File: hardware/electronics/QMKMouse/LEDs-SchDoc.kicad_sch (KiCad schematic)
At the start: 20 parts

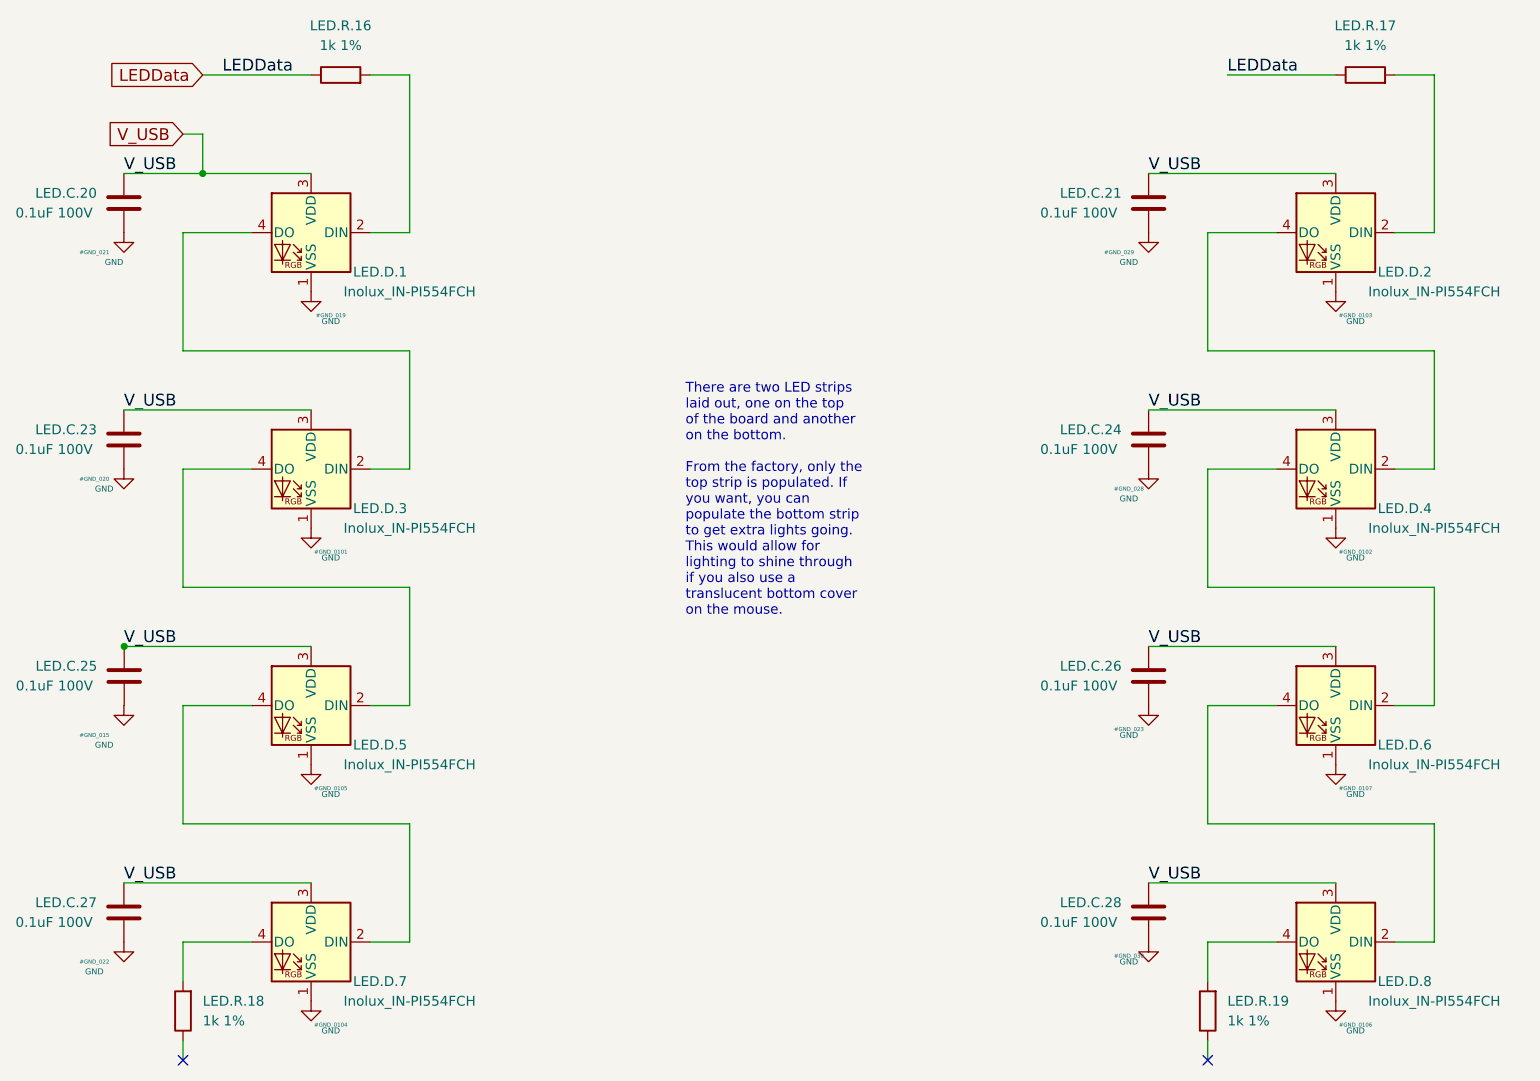
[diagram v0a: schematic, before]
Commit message: update schematic components
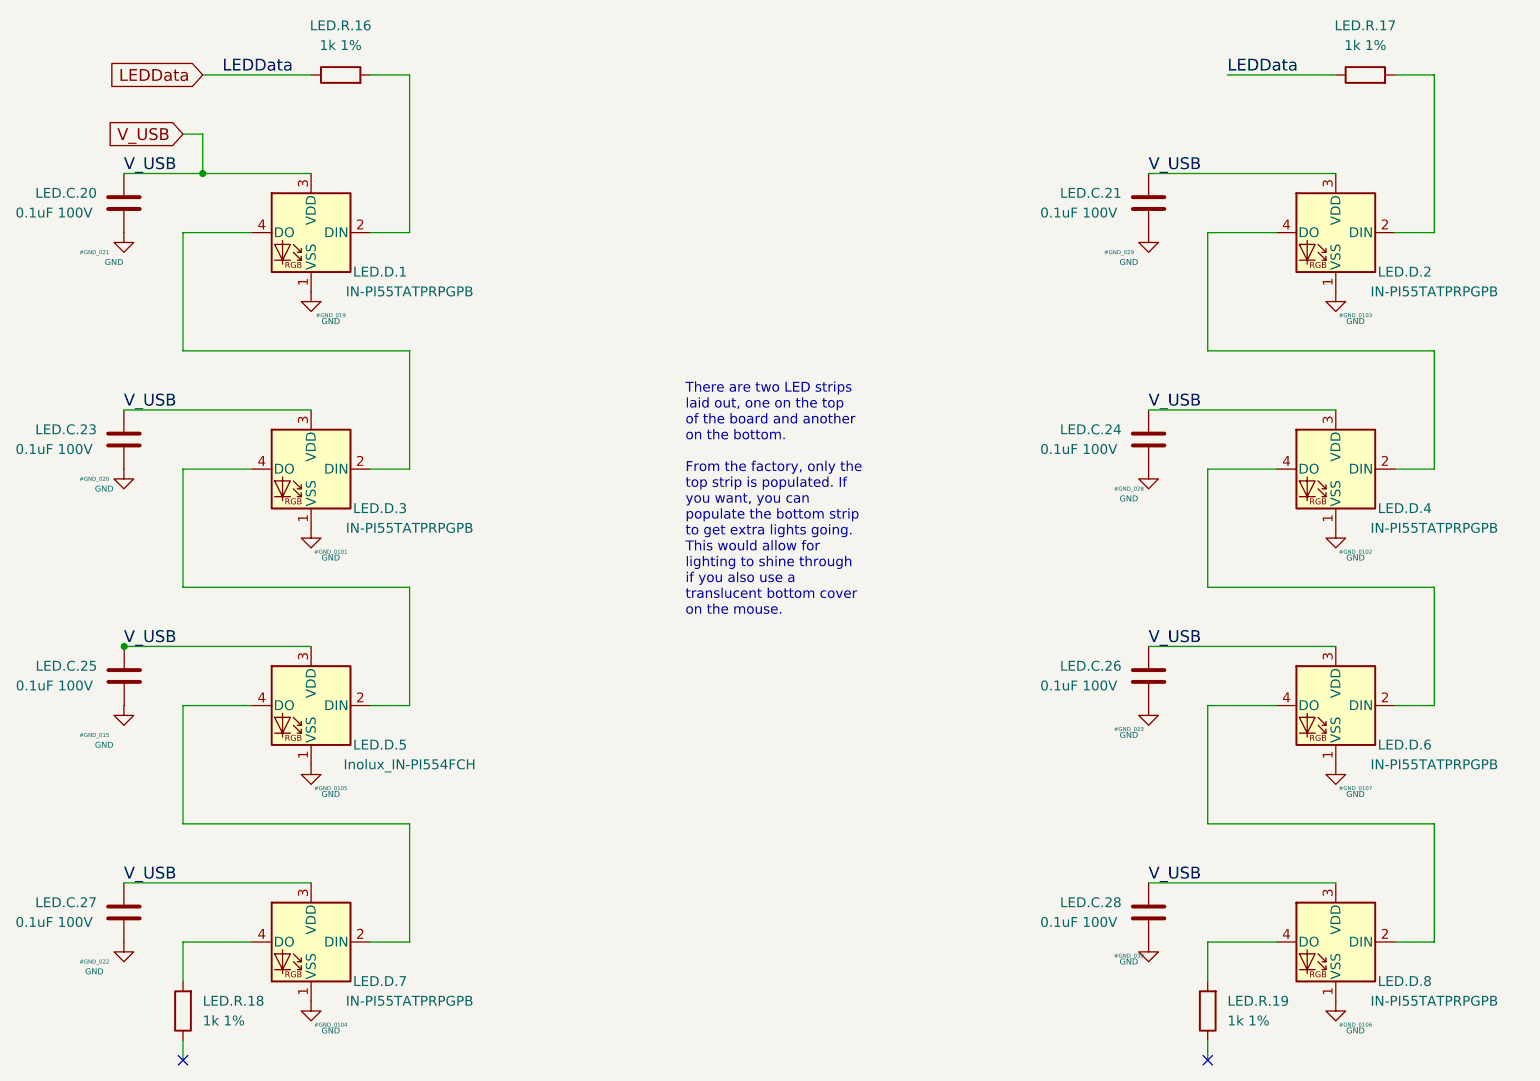
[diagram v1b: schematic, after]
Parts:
- LED.D.1, LED.D.2, LED.D.3, LED.D.4, LED.D.6, LED.D.7, LED.D.8: value Inolux_IN-PI554FCH -> IN-PI55TATPRPGPB
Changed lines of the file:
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@@
     (in_bom yes) (on_board yes)
     (property "Reference" "LED.D.2" (id 0) (at 231.14 55.88 0))
-    (property "Value" "Inolux_IN-PI554FCH" (id 1) (at 234.95 58.42 0))
+    (property "Value" "IN-PI55TATPRPGPB" (id 1) (at 234.95 58.42 0))
     (property "Footprint" "" (id 2) (at 220.98 58.42 0)
       (effects (font (size 1.27 1.27)) (justify left top) hide)
@@
     (in_bom yes) (on_board yes)
     (property "Reference" "LED.D.3" (id 0) (at 99.06 86.36 0))
-    (property "Value" "Inolux_IN-PI554FCH" (id 1) (at 102.87 88.9 0))
+    (property "Value" "IN-PI55TATPRPGPB" (id 1) (at 102.87 88.9 0))
     (property "Footprint" "" (id 2) (at 88.9 88.9 0)
       (effects (font (size 1.27 1.27)) (justify left top) hide)
@@
     (in_bom yes) (on_board yes)
     (property "Reference" "LED.D.1" (id 0) (at 99.06 55.88 0))
-    (property "Value" "Inolux_IN-PI554FCH" (id 1) (at 102.87 58.42 0))
+    (property "Value" "IN-PI55TATPRPGPB" (id 1) (at 102.87 58.42 0))
     (property "Footprint" "" (id 2) (at 88.9 58.42 0)
       (effects (font (size 1.27 1.27)) (justify left top) hide)
@@
     (in_bom yes) (on_board yes)
     (property "Reference" "LED.D.6" (id 0) (at 231.14 116.84 0))
-    (property "Value" "Inolux_IN-PI554FCH" (id 1) (at 234.95 119.38 0))
+    (property "Value" "IN-PI55TATPRPGPB" (id 1) (at 234.95 119.38 0))
     (property "Footprint" "" (id 2) (at 220.98 119.38 0)
       (effects (font (size 1.27 1.27)) (justify left top) hide)
@@
     (in_bom yes) (on_board yes)
     (property "Reference" "LED.D.8" (id 0) (at 231.14 147.32 0))
-    (property "Value" "Inolux_IN-PI554FCH" (id 1) (at 234.95 149.86 0))
+    (property "Value" "IN-PI55TATPRPGPB" (id 1) (at 234.95 149.86 0))
     (property "Footprint" "" (id 2) (at 220.98 149.86 0)
       (effects (font (size 1.27 1.27)) (justify left top) hide)
@@
     (in_bom yes) (on_board yes)
     (property "Reference" "LED.D.7" (id 0) (at 99.06 147.32 0))
-    (property "Value" "Inolux_IN-PI554FCH" (id 1) (at 102.87 149.86 0))
+    (property "Value" "IN-PI55TATPRPGPB" (id 1) (at 102.87 149.86 0))
     (property "Footprint" "" (id 2) (at 88.9 149.86 0)
       (effects (font (size 1.27 1.27)) (justify left top) hide)
@@
     (in_bom yes) (on_board yes)
     (property "Reference" "LED.D.4" (id 0) (at 231.14 86.36 0))
-    (property "Value" "Inolux_IN-PI554FCH" (id 1) (at 234.95 88.9 0))
+    (property "Value" "IN-PI55TATPRPGPB" (id 1) (at 234.95 88.9 0))
     (property "Footprint" "" (id 2) (at 220.98 88.9 0)
       (effects (font (size 1.27 1.27)) (justify left top) hide)

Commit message: update schematic from PCB; sync netlist and fix some symbol orientations; also fix LED symbol
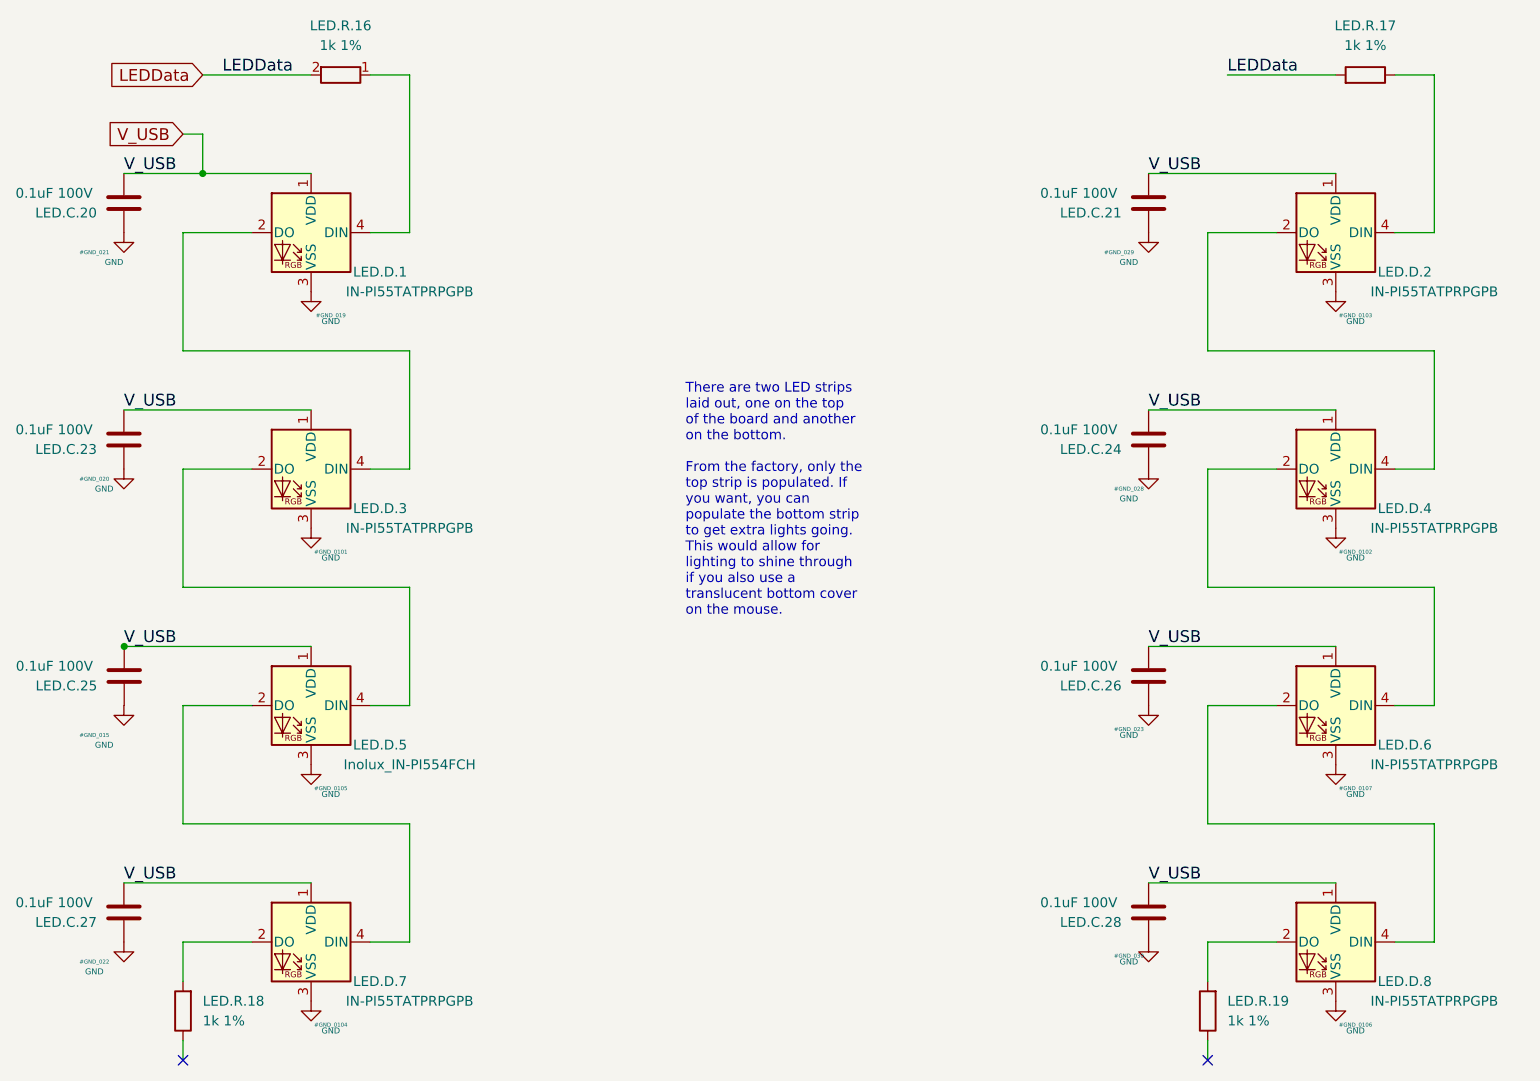
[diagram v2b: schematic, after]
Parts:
- LED.C.20, LED.C.21, LED.C.23, LED.C.24, LED.C.25, LED.C.26, LED.C.27, LED.C.28: footprint Capacitor_SMD:C_0805_2012Metric -> Chip_Passives.PcbLib:0805
- LED.D.1, LED.D.2, LED.D.3, LED.D.4, LED.D.5, LED.D.6, LED.D.7, LED.D.8: footprint (none) -> LED_SMD:LED_WS2812_PLCC6_5.0x5.0mm_P1.6mm; symbol LED:Inolux_IN-PI554FCH -> Mouse_Parts:Inolux_IN-PI55TATPRPGPB
- LED.R.16: footprint (none) -> Chip_Passives.PcbLib:0805
- LED.R.17, LED.R.18, LED.R.19: footprint Resistor_SMD:R_0805_2012Metric -> Chip_Passives.PcbLib:0805
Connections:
- net GND: now also LED.C.20.1, LED.C.21.1, LED.C.23.1, LED.C.24.1, LED.C.26.1, LED.C.27.1, LED.C.28.1, LED.D.1.3 (VSS), LED.D.2.3 (VSS), LED.D.3.3 (VSS), LED.D.4.3 (VSS), LED.D.5.3 (VSS), LED.D.6.3 (VSS), LED.D.7.3 (VSS), LED.D.8.3 (VSS); no longer LED.C.20.2, LED.C.21.2, LED.C.23.2, LED.C.24.2, LED.C.26.2, LED.C.27.2, LED.C.28.2, LED.D.1.1 (VSS), LED.D.2.1 (VSS), LED.D.3.1 (VSS), LED.D.4.1 (VSS), LED.D.5.1 (VSS), LED.D.6.1 (VSS), LED.D.7.1 (VSS), LED.D.8.1 (VSS)
- net LEDData: now also LED.R.16.2, LED.R.17.2; no longer LED.R.16.1, LED.R.17.1
- net V_USB: now also LED.C.20.2, LED.C.21.2, LED.C.23.2, LED.C.24.2, LED.C.25.2, LED.C.26.2, LED.C.27.2, LED.C.28.2, LED.D.1.1 (VDD), LED.D.2.1 (VDD), LED.D.3.1 (VDD), LED.D.4.1 (VDD), LED.D.5.1 (VDD), LED.D.6.1 (VDD), LED.D.7.1 (VDD), LED.D.8.1 (VDD); no longer LED.C.20.1, LED.C.21.1, LED.C.23.1, LED.C.24.1, LED.C.25.1, LED.C.26.1, LED.C.27.1, LED.C.28.1, LED.D.1.3 (VDD), LED.D.2.3 (VDD), LED.D.3.3 (VDD), LED.D.4.3 (VDD), LED.D.5.3 (VDD), LED.D.6.3 (VDD), LED.D.7.3 (VDD), LED.D.8.3 (VDD)
- net at LED.D.2.2 (DO): now also LED.D.4.4 (DIN); no longer LED.R.17.2
- net at LED.D.2.4 (DIN): now also LED.R.17.1; no longer LED.D.4.2 (DIN)
- net at LED.D.3.2 (DO): now also LED.D.5.4 (DIN); no longer LED.D.1.4 (DO)
- net at LED.D.3.4 (DIN): now also LED.D.1.2 (DO); no longer LED.D.5.2 (DIN)
- net at LED.D.7.2 (DO): now also LED.R.18.2; no longer LED.D.5.4 (DO)
- net at LED.R.19.2: now also LED.D.8.2 (DO); no longer LED.D.8.4 (DO)
- net at LED.D.6.2 (DO): now also LED.D.8.4 (DIN); no longer LED.D.4.4 (DO)
- net at LED.D.6.4 (DIN): now also LED.D.4.2 (DO); no longer LED.D.8.2 (DIN)
- net at LED.D.7.4 (DIN): now also LED.D.5.2 (DO); no longer LED.R.18.2
- new net: LED.D.1.4 (DIN), LED.R.16.1
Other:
- moved on the sheet: LED.R.17

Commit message: Fix all remaining DRC errors and schematic mismatches
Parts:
- LED.D.1, LED.D.2, LED.D.3, LED.D.4, LED.D.5, LED.D.6, LED.D.7, LED.D.8: footprint LED_SMD:LED_WS2812_PLCC6_5.0x5.0mm_P1.6mm -> LEDs.PcbLib:IN-PI55TATPRPGPB
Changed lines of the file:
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@@
     (property "Reference" "LED.D.2" (id 0) (at 231.14 55.88 0))
     (property "Value" "IN-PI55TATPRPGPB" (id 1) (at 234.95 58.42 0))
-    (property "Footprint" "LED_SMD:LED_WS2812_PLCC6_5.0x5.0mm_P1.6mm" (id 2) (at 220.98 58.42 0)
+    (property "Footprint" "LEDs.PcbLib:IN-PI55TATPRPGPB" (id 2) (at 220.98 58.42 0)
       (effects (font (size 1.27 1.27)) (justify left top) hide)
     )
@@
     (property "Reference" "LED.D.3" (id 0) (at 99.06 86.36 0))
     (property "Value" "IN-PI55TATPRPGPB" (id 1) (at 102.87 88.9 0))
-    (property "Footprint" "LED_SMD:LED_WS2812_PLCC6_5.0x5.0mm_P1.6mm" (id 2) (at 88.9 88.9 0)
+    (property "Footprint" "LEDs.PcbLib:IN-PI55TATPRPGPB" (id 2) (at 88.9 88.9 0)
       (effects (font (size 1.27 1.27)) (justify left top) hide)
     )
@@
     (property "Reference" "LED.D.1" (id 0) (at 99.06 55.88 0))
     (property "Value" "IN-PI55TATPRPGPB" (id 1) (at 102.87 58.42 0))
-    (property "Footprint" "LED_SMD:LED_WS2812_PLCC6_5.0x5.0mm_P1.6mm" (id 2) (at 88.9 58.42 0)
+    (property "Footprint" "LEDs.PcbLib:IN-PI55TATPRPGPB" (id 2) (at 88.9 58.42 0)
       (effects (font (size 1.27 1.27)) (justify left top) hide)
     )
@@
     (property "Reference" "LED.D.5" (id 0) (at 99.06 116.84 0))
     (property "Value" "Inolux_IN-PI554FCH" (id 1) (at 102.87 119.38 0))
-    (property "Footprint" "LED_SMD:LED_WS2812_PLCC6_5.0x5.0mm_P1.6mm" (id 2) (at 88.9 119.38 0)
+    (property "Footprint" "LEDs.PcbLib:IN-PI55TATPRPGPB" (id 2) (at 88.9 119.38 0)
       (effects (font (size 1.27 1.27)) (justify left top) hide)
     )
@@
     (property "Reference" "LED.D.6" (id 0) (at 231.14 116.84 0))
     (property "Value" "IN-PI55TATPRPGPB" (id 1) (at 234.95 119.38 0))
-    (property "Footprint" "LED_SMD:LED_WS2812_PLCC6_5.0x5.0mm_P1.6mm" (id 2) (at 220.98 119.38 0)
+    (property "Footprint" "LEDs.PcbLib:IN-PI55TATPRPGPB" (id 2) (at 220.98 119.38 0)
       (effects (font (size 1.27 1.27)) (justify left top) hide)
     )
@@
     (property "Reference" "LED.D.8" (id 0) (at 231.14 147.32 0))
     (property "Value" "IN-PI55TATPRPGPB" (id 1) (at 234.95 149.86 0))
-    (property "Footprint" "LED_SMD:LED_WS2812_PLCC6_5.0x5.0mm_P1.6mm" (id 2) (at 220.98 149.86 0)
+    (property "Footprint" "LEDs.PcbLib:IN-PI55TATPRPGPB" (id 2) (at 220.98 149.86 0)
       (effects (font (size 1.27 1.27)) (justify left top) hide)
     )
@@
     (property "Reference" "LED.D.7" (id 0) (at 99.06 147.32 0))
     (property "Value" "IN-PI55TATPRPGPB" (id 1) (at 102.87 149.86 0))
-    (property "Footprint" "LED_SMD:LED_WS2812_PLCC6_5.0x5.0mm_P1.6mm" (id 2) (at 88.9 149.86 0)
+    (property "Footprint" "LEDs.PcbLib:IN-PI55TATPRPGPB" (id 2) (at 88.9 149.86 0)
       (effects (font (size 1.27 1.27)) (justify left top) hide)
     )
@@
     (property "Reference" "LED.D.4" (id 0) (at 231.14 86.36 0))
     (property "Value" "IN-PI55TATPRPGPB" (id 1) (at 234.95 88.9 0))
-    (property "Footprint" "LED_SMD:LED_WS2812_PLCC6_5.0x5.0mm_P1.6mm" (id 2) (at 220.98 88.9 0)
-      (effects (font (size 1.27 1.27)) (justify left top) hide)
-    )
+    (property "Footprint" "LEDs.PcbLib:IN-PI55TATPRPGPB" (id 2) (at 220.98 88.9 0)
+      (effects (font (size 1.27 1.27)) (justify left top) hide)
+    )
